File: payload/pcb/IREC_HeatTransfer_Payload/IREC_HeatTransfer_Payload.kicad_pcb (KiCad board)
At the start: 2 copper layers, 63.5 x 101.6 mm, 53 parts, among them J1 Screw_Terminal_01x06, J2 XT60PW-M, J3 Screw_Terminal_01x06, J4 POWER, J5 GPIO, J6 SPI, J7 I2C, U1 MAX31855KASA, U2 MAX31855KASA, U3 MAX31855KASA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

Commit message: upd
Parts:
- R1: moved to B.Cu
- moved R1 16.2 mm to (184.9, 79.0), turned to 180 degrees
- moved D1 12.3 mm to (184.9, 78.7), turned to 0 degrees
- moved JP1 0.86 mm to (168.3, 75.9), turned to 90 degrees

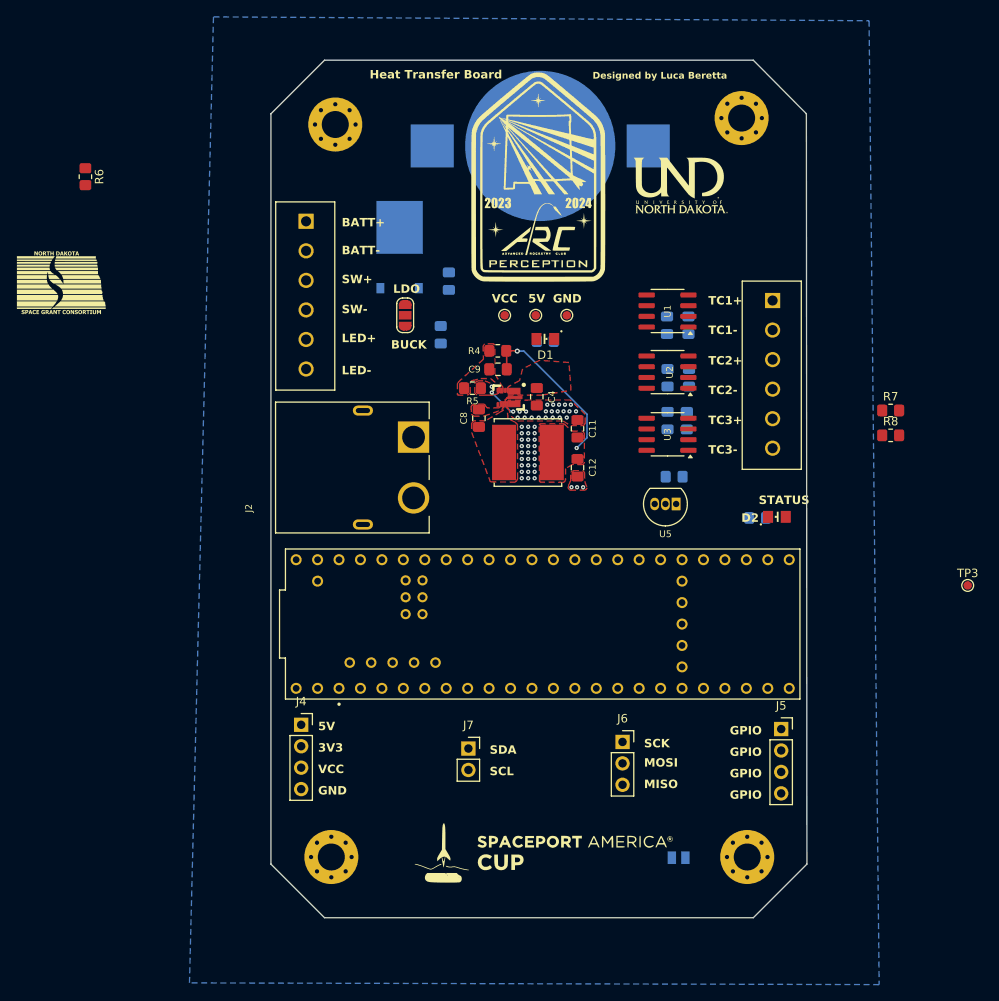
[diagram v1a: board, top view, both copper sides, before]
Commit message: added pitot
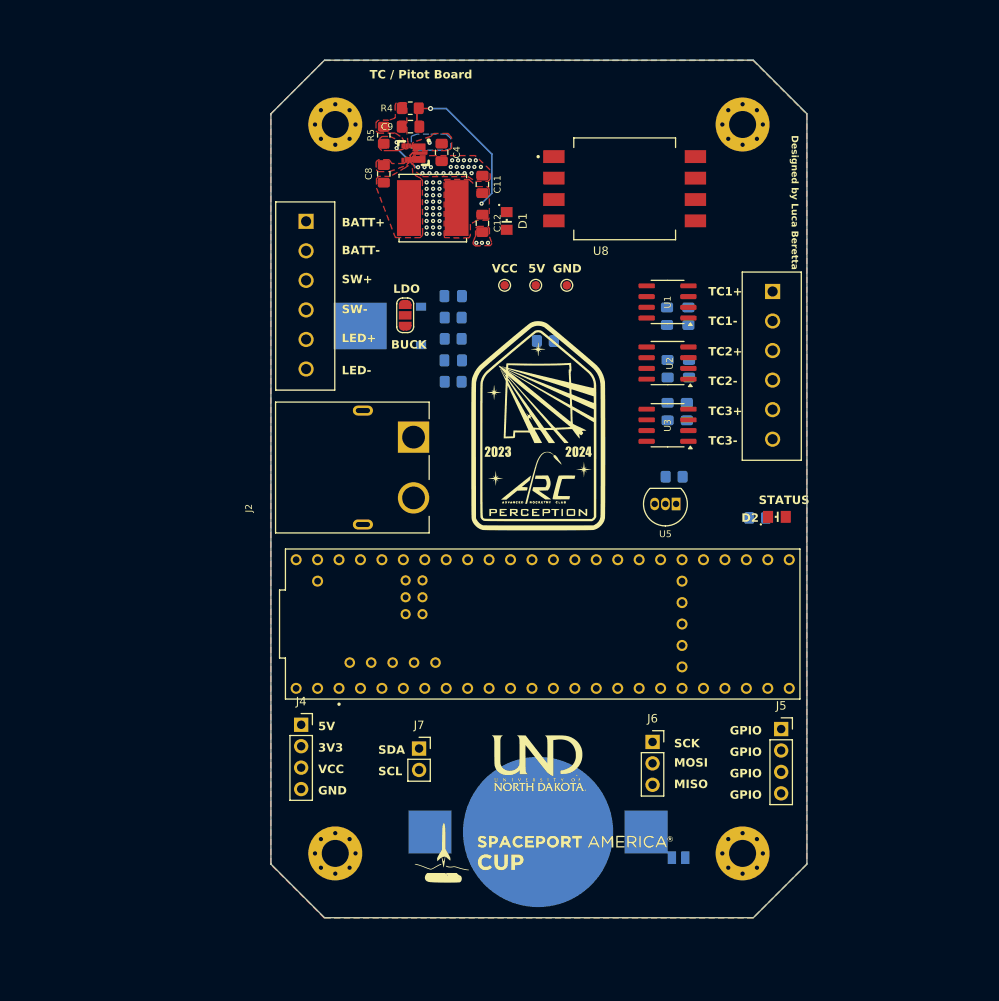
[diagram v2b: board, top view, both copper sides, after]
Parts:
- removed the G*** at (127.6, 72.1)
- removed the TP2 at (180.1, 75.9)
- added U8: MPXV7002DP, SnapEDA Library:XDCR_MPXV7002DP, F.Cu at (194.3, 61.0)
- R6, R7, R8: moved to B.Cu
- moved BT1 81.3 mm to (184.1, 137.2), turned to 0 degrees
- moved G*** 70.5 mm to (184.2, 129.0)
- moved TP3 65.4 mm to (180.1, 72.4)
- moved R8 53.1 mm to (174.0, 78.7), turned to 180 degrees
- moved R7 53.0 mm to (174.0, 76.2)
- moved R6 49.9 mm to (174.0, 83.8), turned to 0 degrees
- moved R5 31.8 mm to (165.8, 54.6), turned to -90 degrees
- moved C8 31.1 mm to (165.8, 59.2)
- moved U4 31.1 mm to (169.3, 56.7)
- moved C11 31.1 mm to (177.5, 60.4)
- moved C4 31.1 mm to (172.6, 56.6)
- moved L1 31.1 mm to (171.6, 63.2)
- moved C12 31.1 mm to (177.5, 65.0)
- moved C9 30.6 mm to (168.9, 53.6)
- moved R4 30.6 mm to (168.9, 51.4)
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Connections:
- U7 pad 16: unconnected-(U7-A2-Pad16) -> /PITOT
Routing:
- net V_BUCK: track 0.00 -> 1.09 mm, vias 0 -> 1
- added copper zone on B.Cu, net V_BUCK
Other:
- outline, holes or cut-outs redrawn
- board text added: "TC / Pitot Board"
- board text removed: "Heat Transfer Board"

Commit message: upd
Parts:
- moved JP2 10.3 mm to (204.9, 130.8)
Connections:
- net /TEMP_SENSE renamed /DS18_TEMP
- net /VBAT_CR2032 renamed /VBAT_COIN
- U7 pad 11: unconnected-(U7-MOSI-Pad11) -> /MOSI
- U7 pad 18: unconnected-(U7-A4-Pad18) -> /I2C_SDA
- U7 pad 19: unconnected-(U7-A5-Pad19) -> /I2C_SCL
- U7 pad 2: /LED_RED -> unconnected-(U7-OUT2-Pad2)
- U7 pad 20: unconnected-(U7-A6-Pad20) -> /T1_CS
- U7 pad 21: unconnected-(U7-A7-Pad21) -> /T2_CS
- U7 pad 22: unconnected-(U7-A8-Pad22) -> /T3_CS
- U7 pad 41: unconnected-(U7-A17-Pad41) -> /LED_GREEN

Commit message: updates
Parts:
- added J9: Serial, Connector_PinSocket_2.54mm:PinSocket_1x02_P2.54mm_Vertical, F.Cu at (155.4, 127.0)
- J2: footprint CustomFootprintLib:AMASS_XT60PW-M -> Connector_AMASS:AMASS_XT60-M_1x02_P7.20mm_Vertical
- moved J4 34.5 mm to (167.6, 91.9)
- moved J2 29.4 mm to (157.5, 65.2), turned to -90 degrees
- moved R6 19.3 mm to (162.6, 99.3)
- moved J3 16.6 mm to (156.6, 81.4)
- moved G*** 0.64 mm to (184.0, 139.7)
- moved J7 0.25 mm to (170.0, 127.0)
- moved G*** 0.08 mm to (184.1, 129.0)
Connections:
- J4 pad 1: +5V -> VCC
- J4 pad 2: +3V3 -> +5V
- J4 pad 3: VCC -> +3V3
- J5 pad 1: /GPIO -> /GPIO2
- J5 pad 2: /GPIO -> /GPIO3
- J5 pad 3: /GPIO -> /GPIO4
- J5 pad 4: /GPIO -> /GPIO5
- J6 pad 2: /SPI_MOSI -> /SPI_MISO
- J6 pad 3: /SPI_MISO -> /SPI_MOSI
- J7 pad 1: /I2C_SDA -> /I2C_SCL
- J7 pad 2: /I2C_SCL -> /I2C_SDA
- U7 pad 0: unconnected-(U7-RX1-Pad0) -> /RX
- U7 pad 1: unconnected-(U7-TX1-Pad1) -> /TX
- U7 pad 11: /MOSI -> /SPI_MOSI
- U7 pad 12: /MISO -> /SPI_MISO
- U7 pad 2: unconnected-(U7-OUT2-Pad2) -> /GPIO2
- U7 pad 23: unconnected-(U7-A9-Pad23) -> /LED_GREEN
- U7 pad 3: /LED_GREEN -> /GPIO3
- U7 pad 4: unconnected-(U7-BCLK2-Pad4) -> /GPIO4
- U7 pad 41: /LED_GREEN -> unconnected-(U7-A17-Pad41)
- U7 pad 5: unconnected-(U7-IN2-Pad5) -> /GPIO5
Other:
- board text added: "RX"
- board text added: "TX"

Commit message: began routing
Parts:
- moved J2 6.95 mm to (157.2, 72.1), turned to 90 degrees
- moved R6 3.89 mm to (161.8, 95.5)
- moved JP1 1.88 mm to (170.2, 75.9)
- moved J6 0.51 mm to (197.1, 126.5)
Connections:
- J5 pad 1: /GPIO2 -> /GPIO27
- J5 pad 2: /GPIO3 -> /GPIO26
- J5 pad 3: /GPIO4 -> /GPIO25
- J5 pad 4: /GPIO5 -> /GPIO24
- JP1 pad 1: V_BUCK -> V_LDO
- JP1 pad 3: V_LDO -> V_BUCK
- U7 pad 13: /SCK -> /SPI_SCK
- U7 pad 2: /GPIO2 -> unconnected-(U7-OUT2-Pad2)
- U7 pad 24: unconnected-(U7-A10-Pad24) -> /GPIO24
- U7 pad 25: unconnected-(U7-A11-Pad25) -> /GPIO25
- U7 pad 26: unconnected-(U7-A12-Pad26) -> /GPIO26
- U7 pad 27: unconnected-(U7-A13-Pad27) -> /GPIO27
- U7 pad 3: /GPIO3 -> unconnected-(U7-LRCLK2-Pad3)
- U7 pad 3.3V_1: +3V3 -> unconnected-(U7-3.3V-Pad3.3V_1)
- U7 pad 3.3V_2: unconnected-(U7-3.3V__1-Pad3.3V_2) -> +3V3
- U7 pad 4: /GPIO4 -> unconnected-(U7-BCLK2-Pad4)
- U7 pad 5: /GPIO5 -> unconnected-(U7-IN2-Pad5)
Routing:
- net /VBAT_COIN: track 0.00 -> 60.5 mm, vias 0 -> 2
- net +5V: track 19.5 -> 74.7 mm
- net VCC: track 0.00 -> 40.6 mm
- net /GPIO24: track 0.00 -> 25.3 mm
- net /GPIO25: track 0.00 -> 20.9 mm
- net +BATT: track 0.00 -> 19.1 mm
- net /SPI_MOSI: track 0.00 -> 17.8 mm
- net /GPIO26: track 0.00 -> 17.3 mm
- net /SPI_MISO: track 0.00 -> 13.7 mm
- net /GPIO27: track 0.00 -> 13.7 mm
- net +3V3: track 0.00 -> 11.7 mm
- net /TX: track 0.00 -> 11.5 mm
- net /LED_GREEN: track 0.00 -> 9.48 mm
- net /RX: track 0.00 -> 7.88 mm
- net Net-(J3-Pin_5): track 0.00 -> 4.26 mm

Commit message: updates
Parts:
- moved R2 14.0 mm to (199.1, 91.2)
- moved R1 13.5 mm to (174.0, 71.1), turned to 0 degrees
- moved C13 7.63 mm to (174.0, 73.7)
- moved C10 7.61 mm to (174.0, 81.3)
- moved R3 6.26 mm to (199.1, 88.9)
- moved U6 4.52 mm to (165.9, 81.5), turned to 0 degrees
- moved C1 3.25 mm to (199.1, 77.8), turned to 0 degrees
- moved C7 2.99 mm to (199.1, 84.4), turned to 180 degrees
- moved C2 2.80 mm to (199.1, 82.2), turned to 0 degrees
- moved C3 2.66 mm to (199.1, 86.6), turned to 0 degrees
- moved C6 2.28 mm to (199.1, 80.0), turned to 180 degrees
- moved JP2 0.56 mm to (204.9, 131.3)
- moved C5 0.45 mm to (199.1, 75.6), turned to 180 degrees
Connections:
- U1 pad 5: /SCK -> /SPI_SCK
- U1 pad 7: /MISO -> /SPI_MISO
- U2 pad 5: /SCK -> /SPI_SCK
- U2 pad 7: /MISO -> /SPI_MISO
- U3 pad 5: /SCK -> /SPI_SCK
- U3 pad 7: /MISO -> /SPI_MISO
- U7 pad 20: /T1_CS -> /T3_CS
- U7 pad 22: /T3_CS -> /T1_CS
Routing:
- net +3V3: track 11.7 -> 113.7 mm, vias 0 -> 5
- net /SPI_SCK: track 0.00 -> 66.6 mm, vias 0 -> 3
- net /T-: track 0.00 -> 63.0 mm, vias 0 -> 3
- net /SPI_MISO: track 13.7 -> 72.3 mm, vias 0 -> 4
- net /LED_GREEN: track 9.48 -> 62.0 mm, vias 0 -> 2
- net /T1_CS: track 0.00 -> 44.7 mm
- net /PITOT: track 0.00 -> 42.3 mm, vias 0 -> 1
- net /T2_CS: track 0.00 -> 38.7 mm
- net +5V: track 74.7 -> 109.2 mm, vias 2 -> 3
- net /T3_CS: track 0.00 -> 33.2 mm
- net /VBAT_SENSE: track 0.00 -> 32.1 mm, vias 0 -> 1
- net /DS18_TEMP: track 0.00 -> 32.0 mm
- net V_BUCK: track 1.09 -> 29.7 mm, vias 1 -> 2
- net /I2C_SDA: track 0.00 -> 28.1 mm
- net /I2C_SCL: track 0.00 -> 24.6 mm
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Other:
- board text added: "Mounting Hole"
- board text removed: "GND Mounting Hole"

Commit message: GPIOs renamed
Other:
- board text added: "GPIO24"
- board text added: "GPIO25"
- board text added: "GPIO26"
- board text added: "GPIO27"
- board text removed: "GPIO"

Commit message: upd
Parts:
- moved BT1 1.02 mm to (184.1, 136.1), turned to 180 degrees
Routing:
- net GND: vias 62 -> 71
